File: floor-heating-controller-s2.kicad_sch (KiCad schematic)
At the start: 3 parts

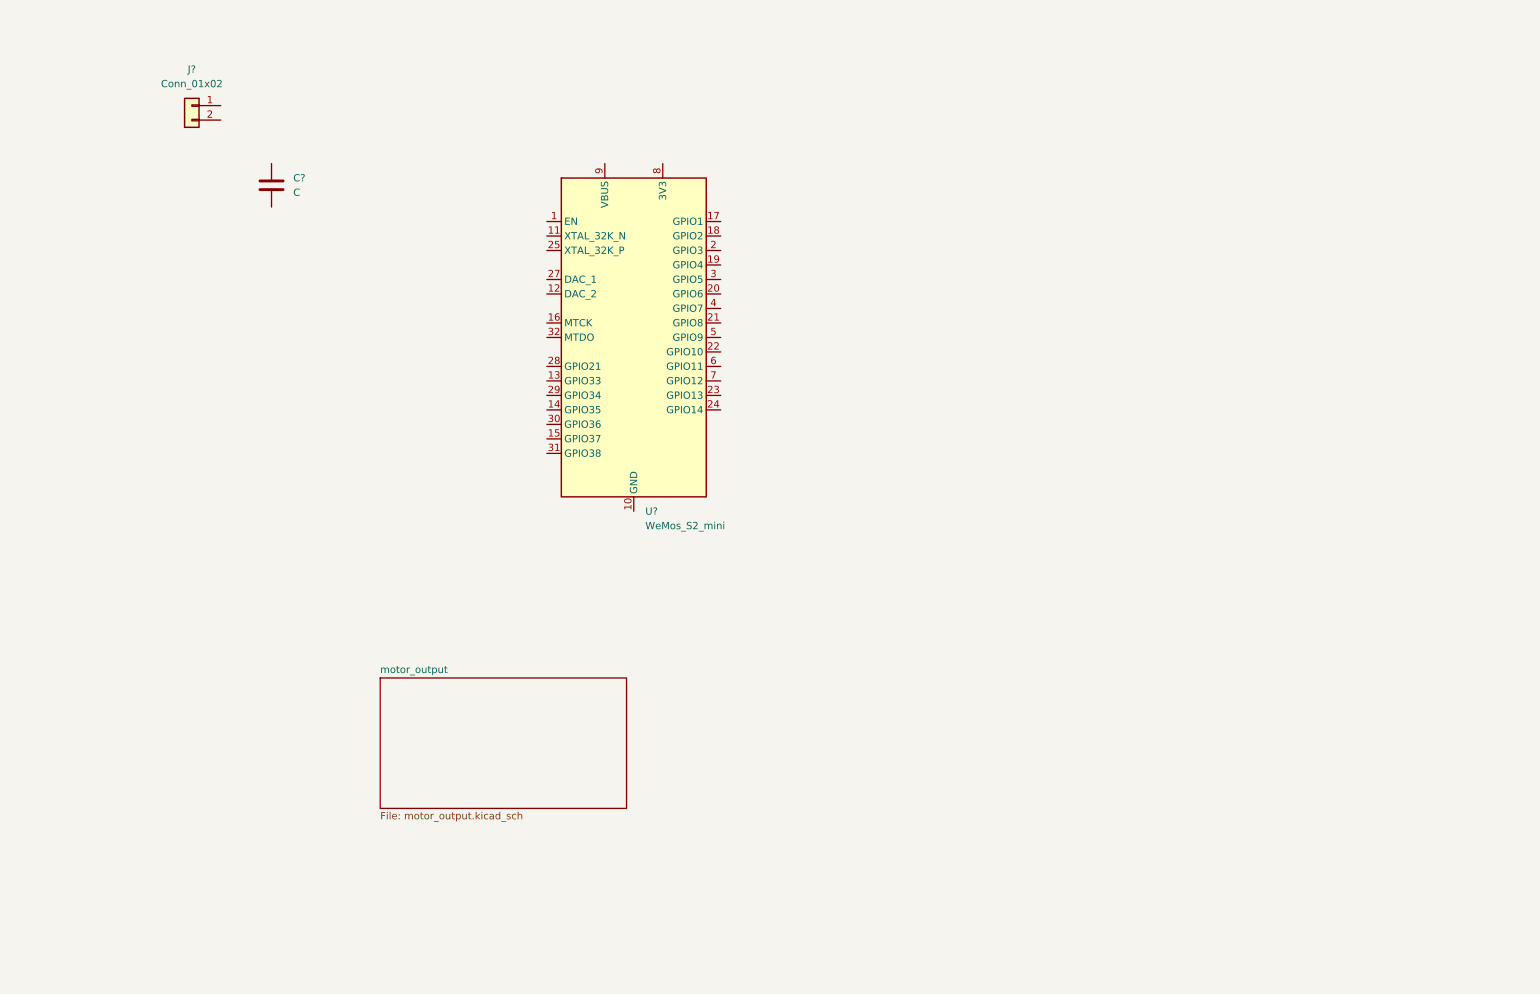
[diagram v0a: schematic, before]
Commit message: changed gain of opamps
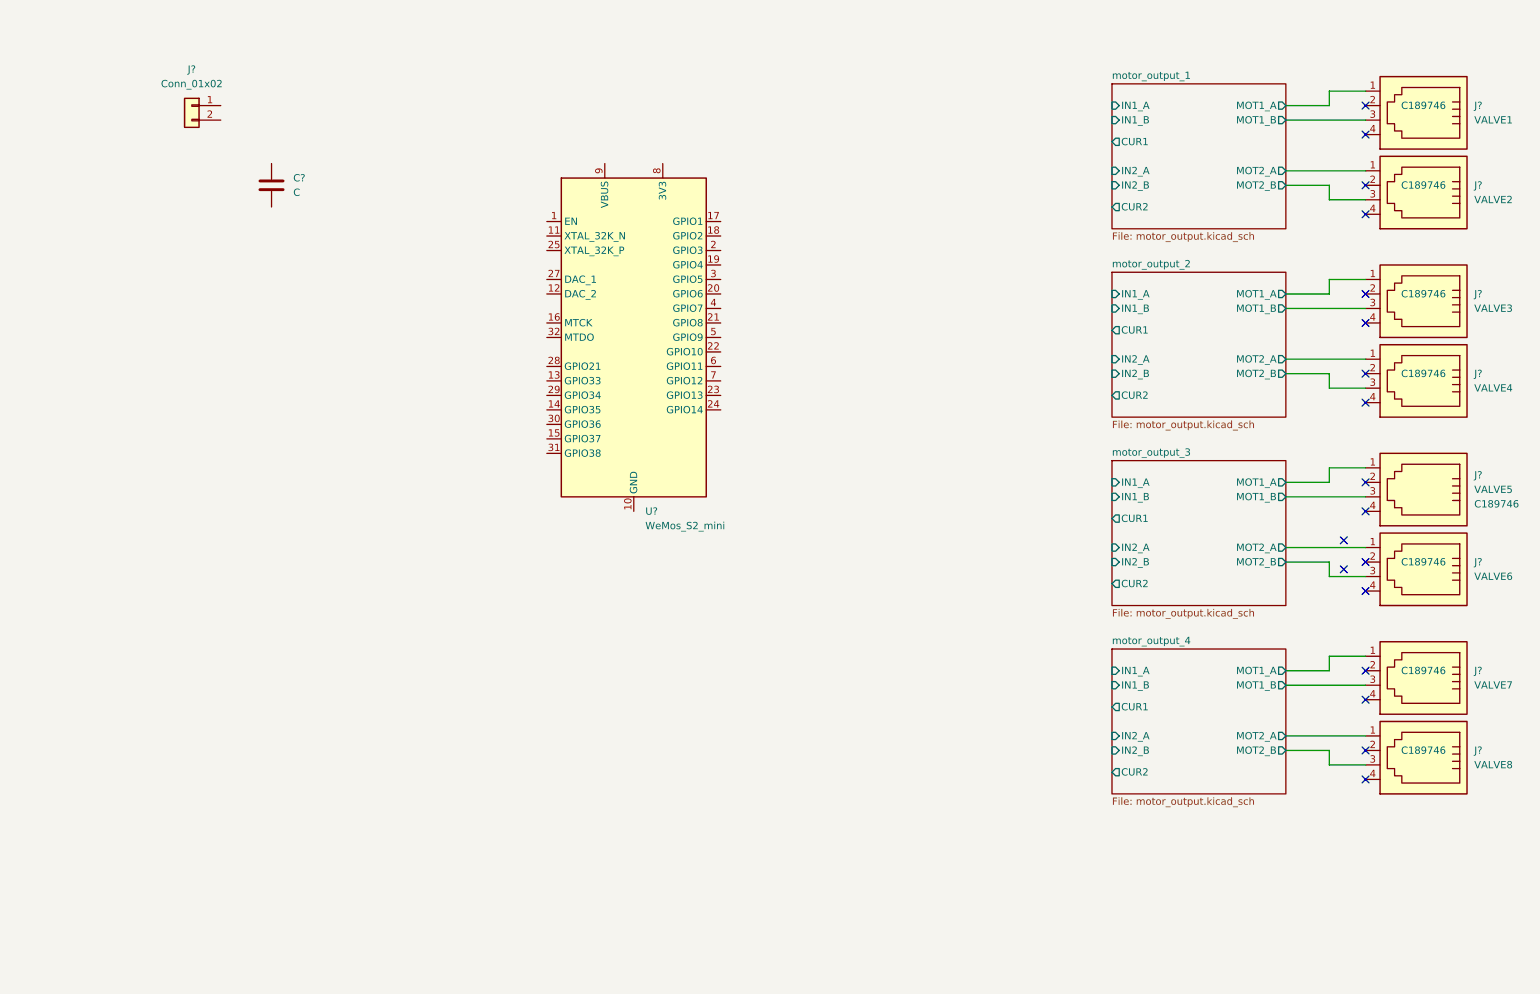
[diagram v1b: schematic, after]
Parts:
- added J?: VALVE8, Connector_RJ:RJ14_Connfly_DS1133-S4_Horizontal, symbol Connector:4P4C
- added J?: VALVE3, Connector_RJ:RJ14_Connfly_DS1133-S4_Horizontal, symbol Connector:4P4C
- added J?: VALVE4, Connector_RJ:RJ14_Connfly_DS1133-S4_Horizontal, symbol Connector:4P4C
- added J?: VALVE1, Connector_RJ:RJ14_Connfly_DS1133-S4_Horizontal, symbol Connector:4P4C
- added J?: VALVE5, Connector_RJ:RJ14_Connfly_DS1133-S4_Horizontal, symbol Connector:4P4C
- added J?: VALVE7, Connector_RJ:RJ14_Connfly_DS1133-S4_Horizontal, symbol Connector:4P4C
- added J?: VALVE2, Connector_RJ:RJ14_Connfly_DS1133-S4_Horizontal, symbol Connector:4P4C
- added J?: VALVE6, Connector_RJ:RJ14_Connfly_DS1133-S4_Horizontal, symbol Connector:4P4C
- J?: footprint (none) -> Connector_JST:JST_PH_B2B-PH-K_1x02_P2.00mm_Vertical
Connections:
- new net motor_output_1/MOT1_A: J?.1
- new net motor_output_1/MOT1_B: J?.3
- new net motor_output_1/MOT2_A: J?.1
- new net motor_output_1/MOT2_B: J?.3
- new net motor_output_2/MOT1_A: J?.1
- new net motor_output_2/MOT1_B: J?.3
- new net motor_output_2/MOT2_A: J?.1
- new net motor_output_2/MOT2_B: J?.3
- new net motor_output_3/MOT1_A: J?.1
- new net motor_output_3/MOT1_B: J?.3
- new net motor_output_3/MOT2_A: J?.1
- new net motor_output_3/MOT2_B: J?.3
- new net motor_output_4/MOT1_A: J?.1
- new net motor_output_4/MOT1_B: J?.3
- new net motor_output_4/MOT2_A: J?.1
- new net motor_output_4/MOT2_B: J?.3
- no-connect marks 0 -> 18
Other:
- sheet motor_output renamed motor_output_1
- added sheet motor_output_2 (motor_output.kicad_sch)
- added sheet motor_output_3 (motor_output.kicad_sch)
- added sheet motor_output_4 (motor_output.kicad_sch)
- sheet motor_output_1 ports: added CUR1, CUR2, IN1_A, IN1_B, IN2_A, IN2_B, MOT1_A, MOT1_B, MOT2_A, MOT2_B; removed none

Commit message: finished schematics
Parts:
- removed C?: C, symbol Device:C
- added C1: 100n, Capacitor_SMD:C_0603_1608Metric, symbol Device:C
- added D1: SS54, Diode_SMD:D_SMA, symbol Device:D_Schottky
- added J18: Conn_01x01, TestPoint:TestPoint_2Pads_Pitch5.08mm_Drill1.3mm, symbol Connector_Generic:Conn_01x02
- added J2: DS18B20_1, Connector_JST:JST_PH_B3B-PH-SM4-TB_1x03-1MP_P2.00mm_Vertical, symbol Connector_Generic:Conn_01x03
- added J3: DS18B20_2, Connector_JST:JST_PH_B3B-PH-SM4-TB_1x03-1MP_P2.00mm_Vertical, symbol Connector_Generic:Conn_01x03
- added J4: DS18B20_3, Connector_JST:JST_PH_B3B-PH-SM4-TB_1x03-1MP_P2.00mm_Vertical, symbol Connector_Generic:Conn_01x03
- added J5: DS18B20_4, Connector_JST:JST_PH_B3B-PH-SM4-TB_1x03-1MP_P2.00mm_Vertical, symbol Connector_Generic:Conn_01x03
- added J6: DS18B20_5, Connector_JST:JST_PH_B3B-PH-SM4-TB_1x03-1MP_P2.00mm_Vertical, symbol Connector_Generic:Conn_01x03
- added J7: DS18B20_6, Connector_JST:JST_PH_B3B-PH-SM4-TB_1x03-1MP_P2.00mm_Vertical, symbol Connector_Generic:Conn_01x03
- added J8: DS18B20_7, Connector_JST:JST_PH_B3B-PH-SM4-TB_1x03-1MP_P2.00mm_Vertical, symbol Connector_Generic:Conn_01x03
- added J9: DS18B20_8, Connector_JST:JST_PH_B3B-PH-SM4-TB_1x03-1MP_P2.00mm_Vertical, symbol Connector_Generic:Conn_01x03
- added R1: 1k, Resistor_SMD:R_0603_1608Metric, symbol Device:R
- added R2: 330R, Resistor_SMD:R_0603_1608Metric, symbol Device:R
- added U1: CJ431, Package_TO_SOT_SMD:SOT-23, symbol Reference_Voltage:TL431DBZ
- J1: renamed from J?; value Conn_01x02 -> Supply; JLCPCB (none) -> C160352
- U2: renamed from U?; footprint Module:WEMOS_S2_mini -> Wemos S2 mini:WEMOS_S2_mini
- gave numbers to parts that had none: 8
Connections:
- net at J1.1 (Pin_1): now also D1.2 (A)
- net GND: now reaches J1.2 (Pin_2)
- net GND: now also U2.10 (GND), U2.26 (GND), C1.2, J2.3 (Pin_3), J3.3 (Pin_3), J4.3 (Pin_3), J5.3 (Pin_3), J6.3 (Pin_3), J7.3 (Pin_3), J8.3 (Pin_3), J9.3 (Pin_3), U1.3 (A)
- net IN4_A: now reaches U2.11 (XTAL_32K_N)
- net IN5_A: now reaches U2.12 (DAC_2)
- net IN6_A: now reaches U2.13 (GPIO33)
- net IN7_A: now reaches U2.14 (GPIO35)
- net IN8_A: now reaches U2.15 (GPIO37)
- net at U2.16 (MTCK): now also J18.2 (Pin_2)
- net CUR1: now reaches U2.17 (GPIO1)
- net CUR2: now reaches U2.18 (GPIO2)
- net CUR4: now reaches U2.19 (GPIO4)
- net CUR3: now reaches U2.2 (GPIO3)
- net CUR6: now reaches U2.20 (GPIO6)
- net CUR8: now reaches U2.21 (GPIO8)
- net IN1_B: now reaches U2.22 (GPIO10)
- net IN3_A: now reaches U2.23 (GPIO13)
- net IN3_B: now reaches U2.24 (GPIO14)
- net DS18B20: now reaches U2.25 (XTAL_32K_P)
- net DS18B20: now also J2.2 (Pin_2), J3.2 (Pin_2), J4.2 (Pin_2), J5.2 (Pin_2), J6.2 (Pin_2), J7.2 (Pin_2), J8.2 (Pin_2), J9.2 (Pin_2), R1.2
- net IN4_B: now reaches U2.27 (DAC_1)
- net IN5_B: now reaches U2.28 (GPIO21)
- net IN6_B: now reaches U2.29 (GPIO34)
- net CUR5: now reaches U2.3 (GPIO5)
- net IN7_B: now reaches U2.30 (GPIO36)
- net IN8_B: now reaches U2.31 (GPIO38)
- net at U2.32 (MTDO): now also J18.1 (Pin_1)
- net CUR7: now reaches U2.4 (GPIO7)
- net IN1_A: now reaches U2.5 (GPIO9)
- net IN2_A: now reaches U2.6 (GPIO11)
- net IN2_B: now reaches U2.7 (GPIO12)
- net +3V3: now reaches U2.8 (3V3)
- net +3V3: now also R1.1
- net +5V: now reaches U2.9 (VBUS)
- net +5V: now also C1.1, D1.1 (K), J2.1 (Pin_1), J3.1 (Pin_1), J4.1 (Pin_1), J5.1 (Pin_1), J6.1 (Pin_1), J7.1 (Pin_1), J8.1 (Pin_1), J9.1 (Pin_1), R2.1
- new net +2V5: R2.2, U1.1 (K), U1.2 (REF)
- no-connect marks 18 -> 19
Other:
- note added: "DS18B20"
- note added: "MCU Module ESP32-S2 Wemos S2 mini compatible"
- note added: "Motor Interface Circuits"
- note added: "Supply 5.5V 1A"
- note added: "Voltage Reference for OpAmps"
- moved on the sheet: J1

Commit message: first placing
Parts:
- J18: value Conn_01x01 -> EXT
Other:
- title: (none) -> Floor Heating Controller S2
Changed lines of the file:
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@@
 (kicad_sch (version 20211123) (generator eeschema)
   (paper "A4")
+  (title_block
+    (title "Floor Heating Controller S2")
+    (date "2022-11-30")
+    (rev "1")
+  )
   (junction (at 63.5 35.56) (diameter 0) (color 0 0 0 0)
   )
@@
     (in_bom yes) (on_board yes)
     (property "Reference" "J18" (id 0) (at 86.36 68.58 90))
-    (property "Value" "Conn_01x01" (id 1) (at 88.9 66.04 0)
-      (effects (font (size 1.27 1.27)) hide)
-    )
+    (property "Value" "EXT" (id 1) (at 88.9 64.77 0))
     (property "Footprint" "TestPoint:TestPoint_2Pads_Pitch5.08mm_Drill1.3mm" (id 2) (at 88.9 69.85 0)
       (effects (font (size 1.27 1.27)) hide)
@@
     )
     (path "/cf6d0f71-082f-417a-a4c9-bd9f7cbc0faf"
-      (reference "J18") (unit 1) (value "Conn_01x01") (footprint "TestPoint:TestPoint_2Pads_Pitch5.08mm_Drill1.3mm")
+      (reference "J18") (unit 1) (value "EXT") (footprint "TestPoint:TestPoint_2Pads_Pitch5.08mm_Drill1.3mm")
     )
     (path "/debddf3b-57ec-419c-9fb2-ac9e95849161"

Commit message: First routing cycle nearly complete
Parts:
- J1: footprint Connector_JST:JST_PH_B2B-PH-K_1x02_P2.00mm_Vertical -> Connector_JST:JST_PH_B2B-PH-SM4-TB_1x02-1MP_P2.00mm_Vertical
- J2, J3, J4, J5, J6, J7, J8, J9: symbol Connector_Generic:Conn_01x03 -> Connector_Generic_MountingPin:Conn_01x03_MountingPin
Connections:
- net GND: now also J2.MP (MountPin), J3.MP (MountPin), J4.MP (MountPin), J5.MP (MountPin), J6.MP (MountPin), J7.MP (MountPin), J8.MP (MountPin), J9.MP (MountPin)
- net motor_output_1/MOT2_A: now also J11.3; no longer J11.1
- net motor_output_1/MOT2_B: now also J11.1; no longer J11.3
- net motor_output_2/MOT1_A: now also J12.3; no longer J12.1
- net motor_output_2/MOT1_B: now also J12.1; no longer J12.3
- net motor_output_2/MOT2_A: now also J13.3; no longer J13.1
- net motor_output_2/MOT2_B: now also J13.1; no longer J13.3
- net motor_output_3/MOT1_A: now also J14.3; no longer J14.1
- net motor_output_3/MOT1_B: now also J14.1; no longer J14.3
- net motor_output_3/MOT2_A: now also J15.3; no longer J15.1
- net motor_output_3/MOT2_B: now also J15.1; no longer J15.3
- net motor_output_4/MOT1_A: now also J16.3; no longer J16.1
- net motor_output_4/MOT1_B: now also J16.1; no longer J16.3

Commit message: production ready
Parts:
- J1: symbol Connector_Generic:Conn_01x02 -> Connector_Generic_MountingPin:Conn_01x02_MountingPin
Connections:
- net GND: now also J1.MP (MountPin)
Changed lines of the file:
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@@
   (junction (at 133.35 143.51) (diameter 0) (color 0 0 0 0)
+  )
+  (junction (at 31.75 33.02) (diameter 0) (color 0 0 0 0)
   )
   (junction (at 91.44 173.99) (diameter 0) (color 0 0 0 0)
@@
     (stroke (width 0) (type default) (color 0 0 0 0))
   )
-  (wire (pts (xy 31.75 25.4) (xy 31.75 36.83))
+  (wire (pts (xy 20.32 33.02) (xy 31.75 33.02))
+    (stroke (width 0) (type default) (color 0 0 0 0))
+  )
+  (wire (pts (xy 31.75 25.4) (xy 31.75 33.02))
     (stroke (width 0) (type default) (color 0 0 0 0))
   )
@@
     (stroke (width 0) (type default) (color 0 0 0 0))
   )
+  (wire (pts (xy 93.98 69.85) (xy 105.41 69.85))
+    (stroke (width 0) (type default) (color 0 0 0 0))
+  )
   (wire (pts (xy 191.77 80.01) (xy 204.47 80.01))
     (stroke (width 0) (type default) (color 0 0 0 0))
@@
     (stroke (width 0) (type default) (color 0 0 0 0))
   )
+  (wire (pts (xy 31.75 33.02) (xy 31.75 36.83))
+    (stroke (width 0) (type default) (color 0 0 0 0))
+  )
   (wire (pts (xy 21.59 147.32) (xy 33.02 147.32))
     (stroke (width 0) (type default) (color 0 0 0 0))
@@
     (stroke (width 0) (type default) (color 0 0 0 0))
   )
+  (wire (pts (xy 20.32 30.48) (xy 20.32 33.02))
+    (stroke (width 0) (type default) (color 0 0 0 0))
+  )
   (polyline (pts (xy 176.53 12.7) (xy 176.53 166.37))
     (stroke (width 0) (type default) (color 0 0 0 0))
@@
     (stroke (width 0) (type default) (color 0 0 0 0))
   )
-  (wire (pts (xy 20.32 36.83) (xy 20.32 34.29))
-    (stroke (width 0) (type default) (color 0 0 0 0))
-  )
   (wire (pts (xy 242.57 128.27) (xy 242.57 125.73))
     (stroke (width 0) (type default) (color 0 0 0 0))
@@
   )
   (wire (pts (xy 71.12 35.56) (xy 71.12 20.32))
-    (stroke (width 0) (type default) (color 0 0 0 0))
-  )
-  (wire (pts (xy 93.98 69.85) (xy 105.41 69.85))
     (stroke (width 0) (type default) (color 0 0 0 0))
   )
@@
     )
   )
-  (symbol (lib_id "power:PWR_FLAG") (at 20.32 34.29 0) (unit 1)
-    (in_bom yes) (on_board yes) (fields_autoplaced)
-    (property "Reference" "#FLG0103" (id 0) (at 20.32 32.385 0)
-      (effects (font (size 1.27 1.27)) hide)
-    )
-    (property "Value" "PWR_FLAG" (id 1) (at 20.32 29.21 0))
-    (property "Footprint" "" (id 2) (at 20.32 34.29 0)
-      (effects (font (size 1.27 1.27)) hide)
-    )
-    (property "Datasheet" "~" (id 3) (at 20.32 34.29 0)
+  (symbol (lib_id "power:PWR_FLAG") (at 20.32 36.83 0) (unit 1)
+    (in_bom yes) (on_board yes)
+    (property "Reference" "#FLG0103" (id 0) (at 20.32 34.925 0)
+      (effects (font (size 1.27 1.27)) hide)
+    )
+    (property "Value" "PWR_FLAG" (id 1) (at 17.78 36.83 90))
+    (property "Footprint" "" (id 2) (at 20.32 36.83 0)
+      (effects (font (size 1.27 1.27)) hide)
+    )
+    (property "Datasheet" "~" (id 3) (at 20.32 36.83 0)
       (effects (font (size 1.27 1.27)) hide)
     )
@@
     (pin "MP")
   )
-  (symbol (lib_id "Connector_Generic:Conn_01x02") (at 20.32 22.86 0) (mirror y) (unit 1)
+  (symbol (lib_id "Connector_Generic_MountingPin:Conn_01x02_MountingPin") (at 20.32 22.86 0) (mirror y) (unit 1)
     (in_bom yes) (on_board yes)
     (property "Reference" "J1" (id 0) (at 20.32 15.24 0))
@@
     (pin "1")
     (pin "2")
+    (pin "MP")
   )
   (symbol (lib_id "power:+5V") (at 33.02 106.68 0) (unit 1)
